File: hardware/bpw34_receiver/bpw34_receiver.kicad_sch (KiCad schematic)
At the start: 25 parts, among them J1 A2 / RED, J2 A0 / IR, J3 ADS1115: RED/GND/IR/GND, U1 OPA333AIDBVR, U2 OPA333AIDBVR

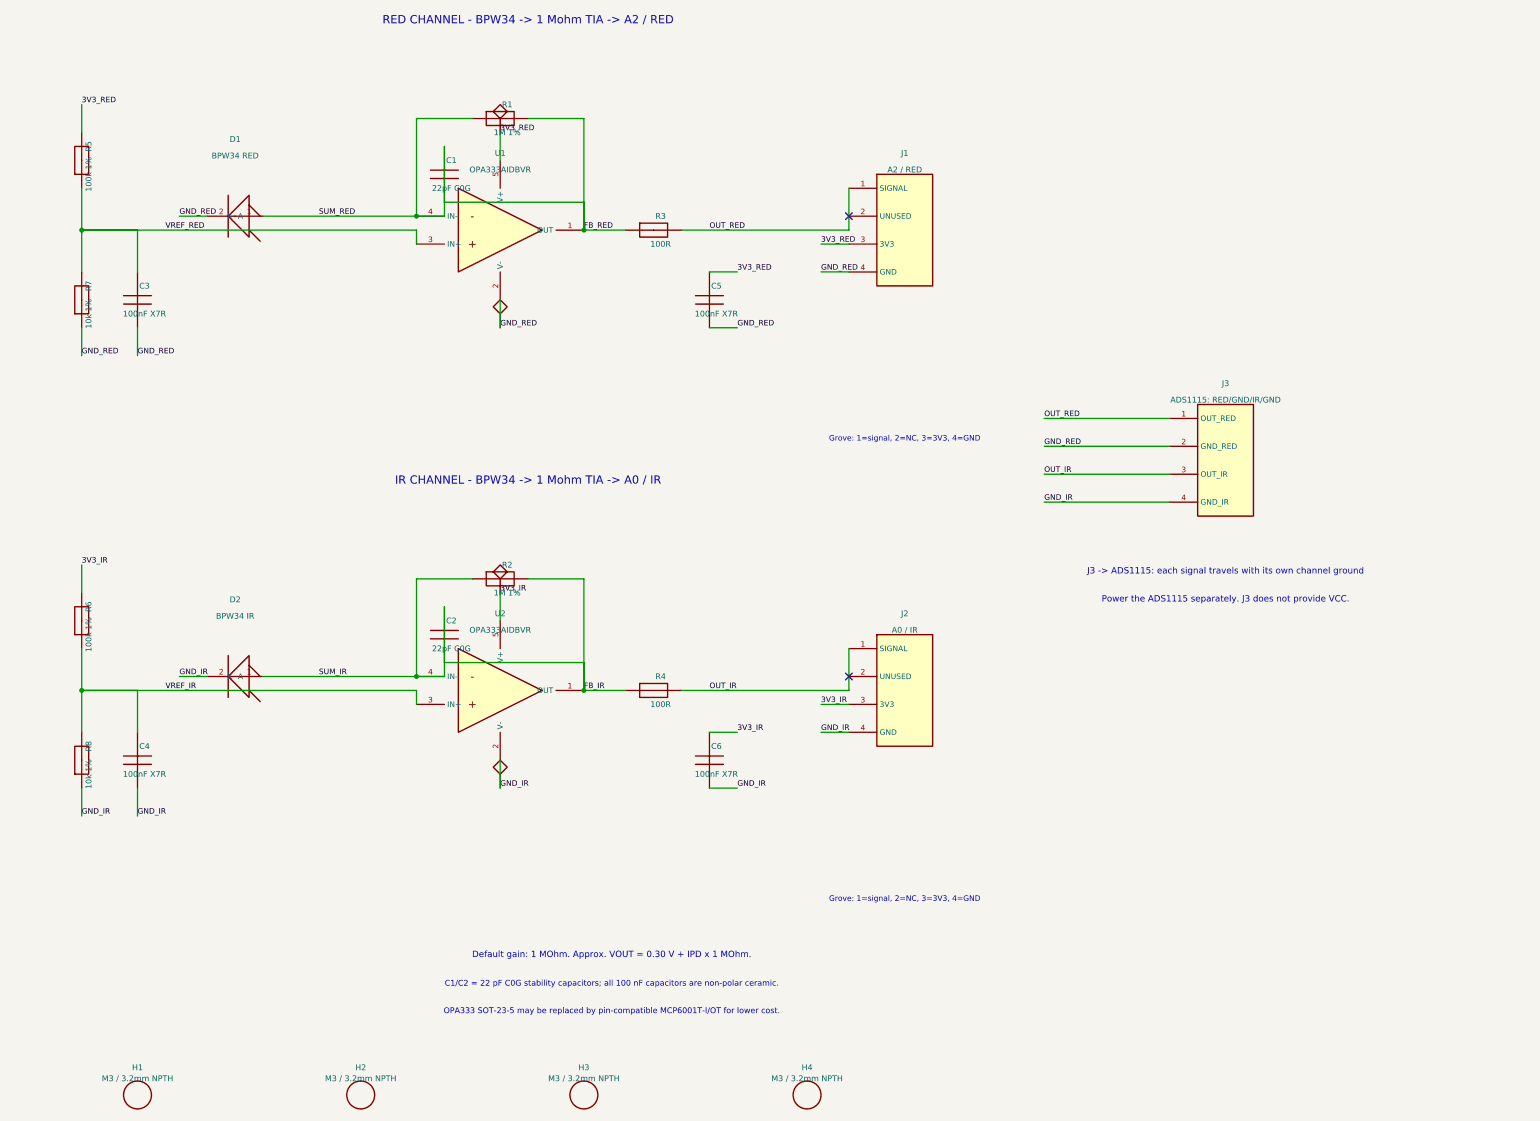
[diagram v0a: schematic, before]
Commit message: hardware: clarify BPW34 schematic and route supplies clear of mounting holes
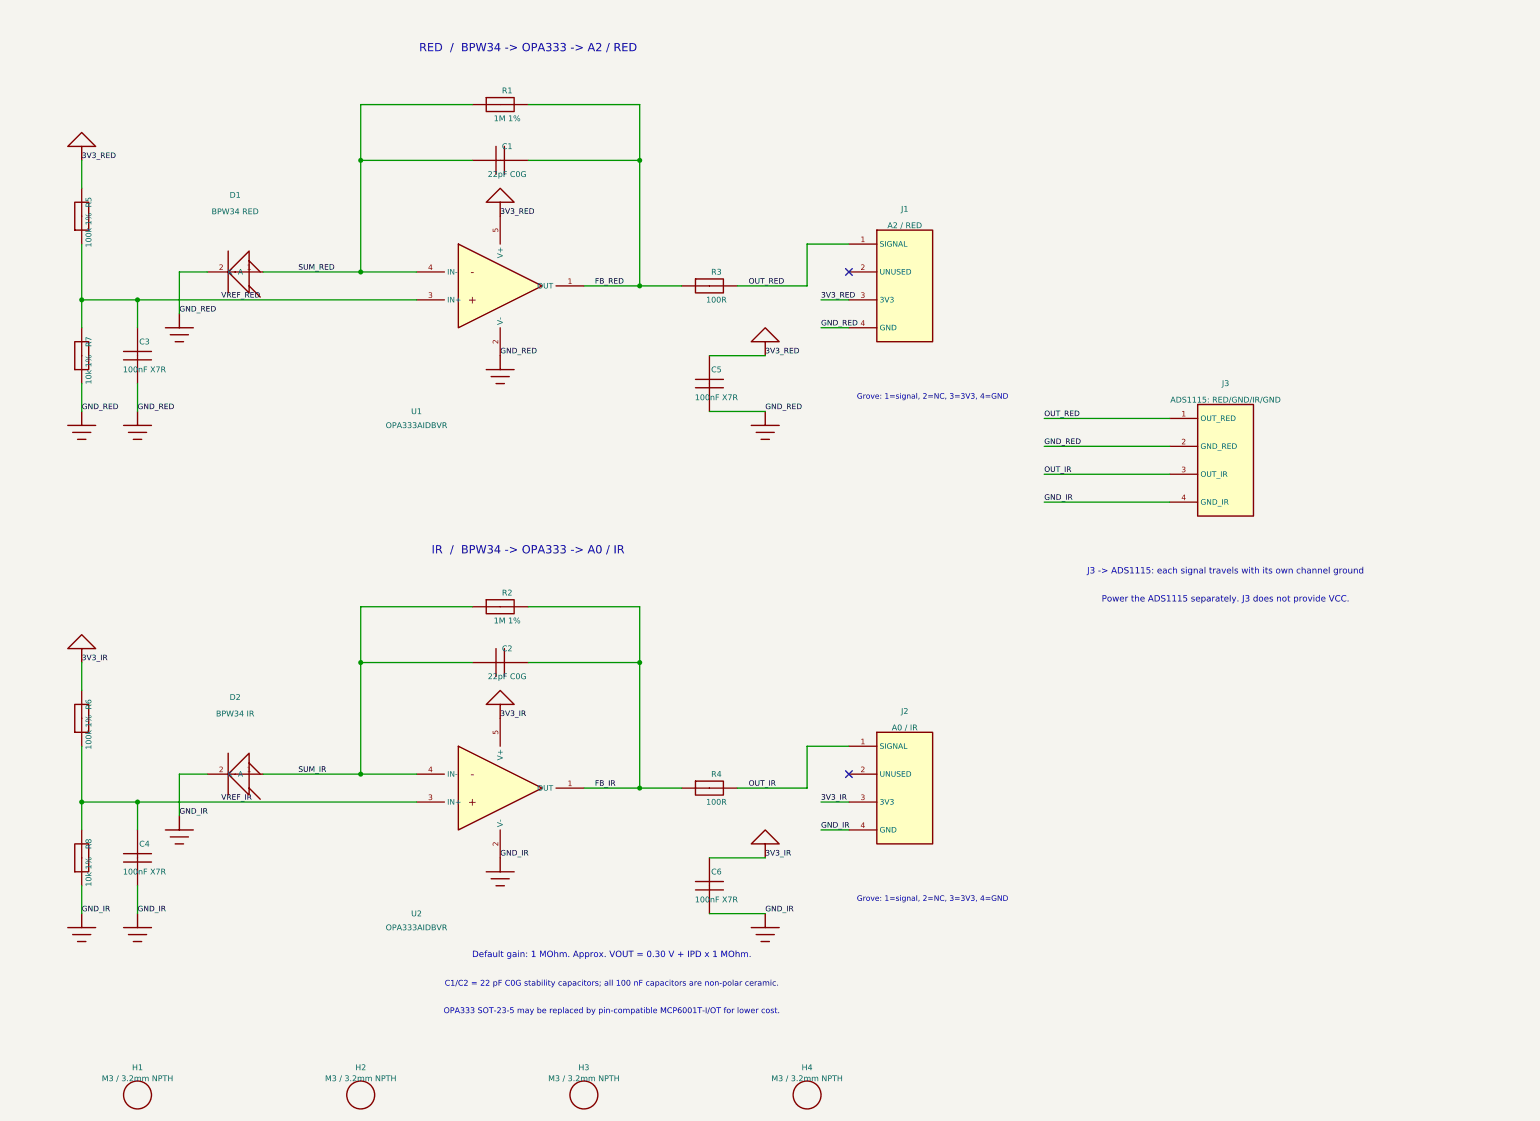
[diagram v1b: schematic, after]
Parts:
- C1, C2: symbol PPG:C -> PPG:CF
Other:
- note added: "IR / BPW34 -> OPA333 -> A0 / IR"
- note added: "RED / BPW34 -> OPA333 -> A2 / RED"
- note removed: "IR CHANNEL - BPW34 -> 1 Mohm TIA -> A0 / IR"
- note removed: "RED CHANNEL - BPW34 -> 1 Mohm TIA -> A2 / RED"
- moved on the sheet: C1, C2, C3, C4, C5, C6, D1, D2, J1, J2, R1, R2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

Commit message: Compact PPG boards, add receiver filters and package V-cut panel
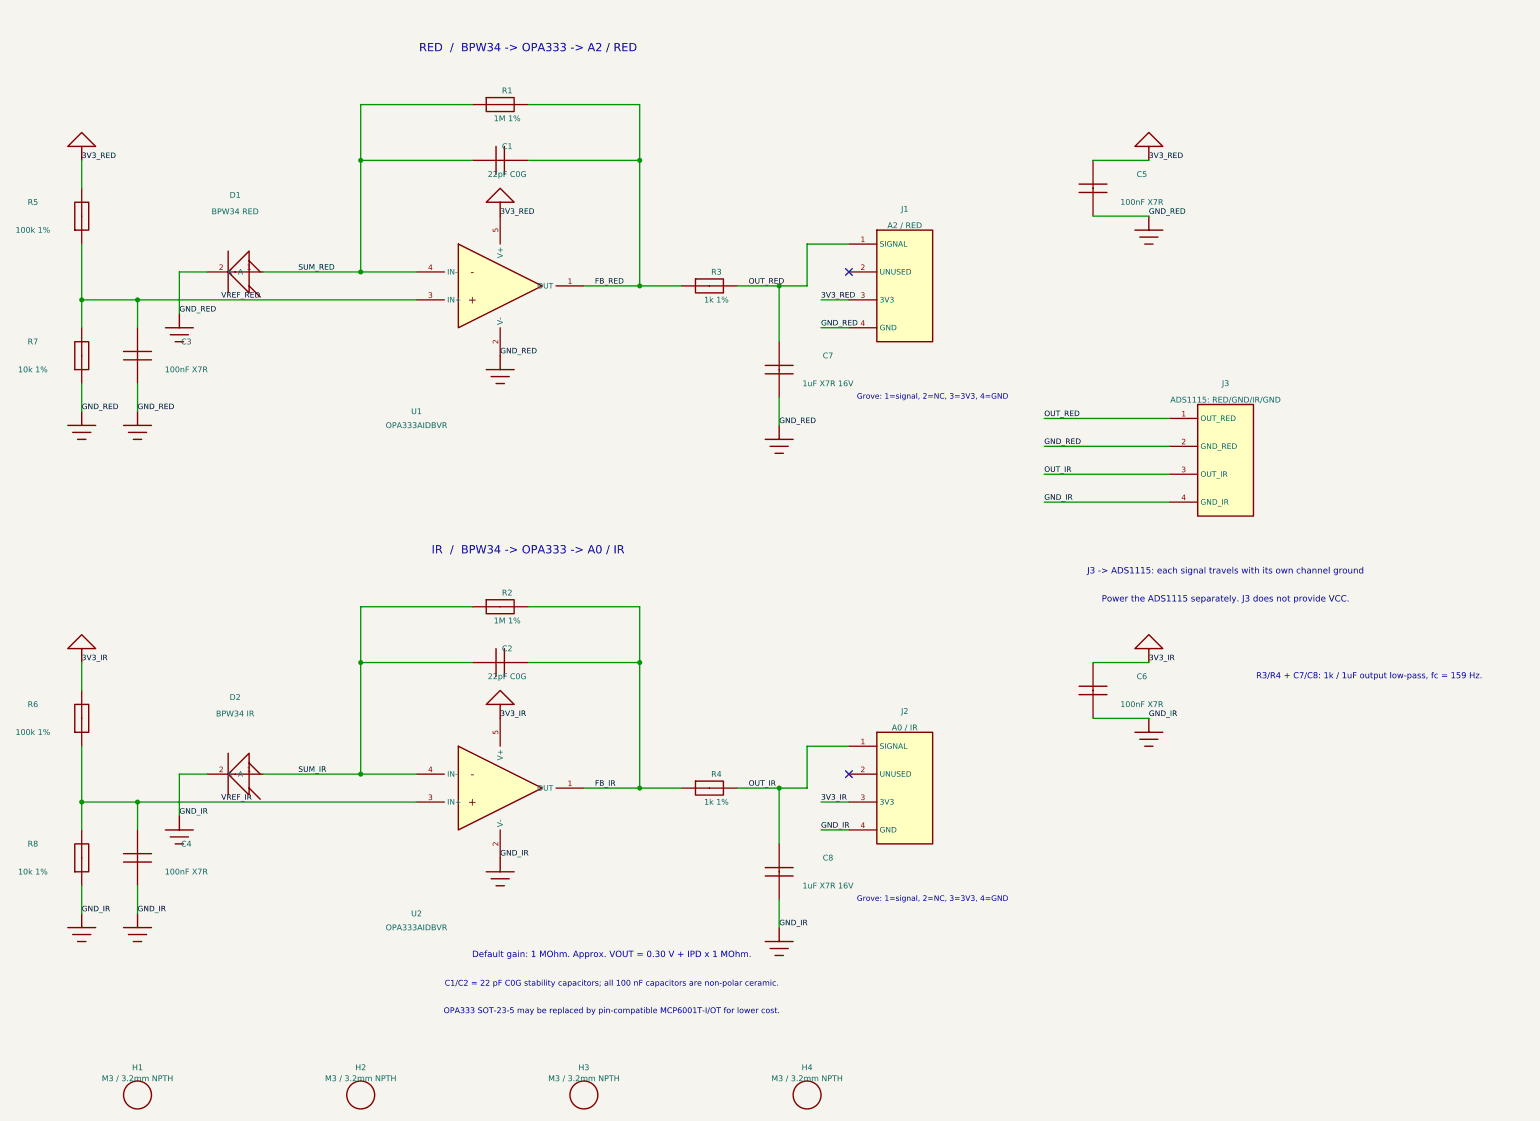
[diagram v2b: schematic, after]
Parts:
- added C7, C8: 1uF X7R 16V, PPG:C0805_Hand, symbol PPG:C
- R3, R4: value 100R -> 1k 1%
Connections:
- net GND_IR: now also C8.2
- net GND_RED: now also C7.2
- net OUT_IR: now also C8.1
- net OUT_RED: now also C7.1
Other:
- note added: "R3/R4 + C7/C8: 1k / 1uF output low-pass, fc = 159 Hz."
- moved on the sheet: C5, C6

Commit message: Shrink PPG receivers to 70x20 and driver to 70x40; refresh V-cut release
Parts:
- removed H1, H2, H3, H4: M3 / 3.2mm NPTH, PPG:MountingHole_M3, symbol PPG:MountingHole
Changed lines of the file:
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@@
 (kicad_sch (version 20250114) (generator "eeschema") (paper "A3")
-(title_block (title "DATN: PPG-Simulator - Dual BPW34 receiver") (date "2026-09-29") (rev "1.3") (comment 1 "Nguyen Nhat Huy - Pham Thanh Vy") (comment 2 "70 x 30 mm / Grove A2 RED + A0 IR / ADS1115 output"))
+(title_block (title "DATN: PPG-Simulator - Dual BPW34 receiver") (date "2026-10-02") (rev "1.4") (comment 1 "Nguyen Nhat Huy - Pham Thanh Vy") (comment 2 "70 x 20 mm / Grove A2 RED + A0 IR / ADS1115 output"))
 (text "RED  /  BPW34 -> OPA333 -> A2 / RED" (at 116.84 40.63999999999999 0) (effects (font (size 1.5 1.5))))
 (symbol (lib_id "PPG:BPW34") (at 63.5 81.27999999999999 0) (unit 1) (in_bom yes) (on_board yes) (dnp no)
@@
 (text "C1/C2 = 22 pF C0G stability capacitors; all 100 nF capacitors are non-polar ceramic." (at 132.08 211.0 0) (effects (font (size 1.05 1.05))))
 (text "OPA333 SOT-23-5 may be replaced by pin-compatible MCP6001T-I/OT for lower cost." (at 132.08 216.0 0) (effects (font (size 1.05 1.05))))
-(symbol (lib_id "PPG:MountingHole") (at 45.72 231.14 0) (unit 1) (in_bom yes) (on_board yes) (dnp no)
-(property "Reference" "H1" (at 45.72 226.14 0) (effects (font (size 1.05 1.05)) ))
-(property "Value" "M3 / 3.2mm NPTH" (at 45.72 228.14 0) (effects (font (size 1.05 1.05)) ))
-(property "Footprint" "PPG:MountingHole_M3" (at 45.72 228.14 0) (effects (font (size 1.05 1.05)) (hide yes)))
-(instances (project "bpw34_receiver" (path "/9e5cca26-1b27-567b-859c-2a64dcbb9a45" (reference "H1") (unit 1)))))
-(symbol (lib_id "PPG:MountingHole") (at 86.36 231.14 0) (unit 1) (in_bom yes) (on_board yes) (dnp no)
-(property "Reference" "H2" (at 86.36 226.14 0) (effects (font (size 1.05 1.05)) ))
-(property "Value" "M3 / 3.2mm NPTH" (at 86.36 228.14 0) (effects (font (size 1.05 1.05)) ))
-(property "Footprint" "PPG:MountingHole_M3" (at 86.36 228.14 0) (effects (font (size 1.05 1.05)) (hide yes)))
-(instances (project "bpw34_receiver" (path "/9e5cca26-1b27-567b-859c-2a64dcbb9a45" (reference "H2") (unit 1)))))
-(symbol (lib_id "PPG:MountingHole") (at 127 231.14 0) (unit 1) (in_bom yes) (on_board yes) (dnp no)
-(property "Reference" "H3" (at 127 226.14 0) (effects (font (size 1.05 1.05)) ))
-(property "Value" "M3 / 3.2mm NPTH" (at 127 228.14 0) (effects (font (size 1.05 1.05)) ))
-(property "Footprint" "PPG:MountingHole_M3" (at 127 228.14 0) (effects (font (size 1.05 1.05)) (hide yes)))
-(instances (project "bpw34_receiver" (path "/9e5cca26-1b27-567b-859c-2a64dcbb9a45" (reference "H3") (unit 1)))))
-(symbol (lib_id "PPG:MountingHole") (at 167.64 231.14 0) (unit 1) (in_bom yes) (on_board yes) (dnp no)
-(property "Reference" "H4" (at 167.64 226.14 0) (effects (font (size 1.05 1.05)) ))
-(property "Value" "M3 / 3.2mm NPTH" (at 167.64 228.14 0) (effects (font (size 1.05 1.05)) ))
-(property "Footprint" "PPG:MountingHole_M3" (at 167.64 228.14 0) (effects (font (size 1.05 1.05)) (hide yes)))
-(instances (project "bpw34_receiver" (path "/9e5cca26-1b27-567b-859c-2a64dcbb9a45" (reference "H4") (unit 1)))))
 (sheet_instances (path "/" (page "1")))
 )
